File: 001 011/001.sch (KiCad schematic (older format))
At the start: 8 parts, among them J1 USB_C_Receptacle_USB2.0, J2 Conn_01x14, J3 Conn_01x12

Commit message: Updated 011 to have the hopefully correct schematic Still a split board bridge the tiny resistor pad for LED function on 001
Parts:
- removed R3, R4: Comp, Resistor_SMD:R_0603_1608Metric_Pad0.98x0.95mm_HandSolder, symbol Device:R
- added R5: Bridge for 001, Resistor_SMD:R_0201_0603Metric, symbol Device:R_Small
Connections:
- net VCC: now also J3.5 (Pin_5), J3.6 (Pin_6), R5.2; no longer D1.1, D1.2, D1.6, D1.7, J3.8 (Pin_8)
- net d+: now also J1.A6 (D+), J1.B6 (D+)
- net d-: now also J1.A7 (D-), J1.B7 (D-)
- new net Annode: D1.1, D1.2, D1.6, D1.7, J3.8 (Pin_8), R5.1
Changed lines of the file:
@@
-$EndComp
-$Comp
-L Connector_Generic:Conn_01x14 J2
-U 1 1 611858EF
-P 3700 1600
-F 0 "J2" H 3780 1592 50  0000 L CNN
-F 1 "Conn_01x14" H 3780 1501 50  0000 L CNN
-F 2 "Molex 503480-1400:503480-1400" H 3700 1600 50  0001 C CNN
-F 3 "~" H 3700 1600 50  0001 C CNN
-	1    3700 1600
-	1    0    0    -1
 $EndComp
 $Comp
@@
 	0    1    1    0
 $EndComp
-$Comp
-L Device:R R3
-U 1 1 61187F93
-P 2150 1500
-F 0 "R3" V 2050 1500 50  0000 C CNN
-F 1 "Comp" V 2150 1500 50  0000 C CNN
-F 2 "Resistor_SMD:R_0603_1608Metric_Pad0.98x0.95mm_HandSolder" V 2080 1500 50  0001 C CNN
-F 3 "~" H 2150 1500 50  0001 C CNN
-	1    2150 1500
-	0    1    1    0
-$EndComp
-$Comp
-L Device:R R4
-U 1 1 611891C9
-P 2150 1700
-F 0 "R4" V 2250 1700 50  0000 C CNN
-F 1 "Comp" V 2150 1700 50  0000 C CNN
-F 2 "Resistor_SMD:R_0603_1608Metric_Pad0.98x0.95mm_HandSolder" V 2080 1700 50  0001 C CNN
-F 3 "~" H 2150 1700 50  0001 C CNN
-	1    2150 1700
-	0    1    1    0
-$EndComp
-Text Label 2400 1500 0    50   ~ 0
+Text Label 1800 1500 0    50   ~ 0
 d-
-Text Label 2400 1700 0    50   ~ 0
+Text Label 1800 1700 0    50   ~ 0
 d+
-Wire Wire Line
-	1700 1450 1700 1500
-Wire Wire Line
-	2000 1500 1700 1500
-Connection ~ 1700 1500
-Wire Wire Line
-	1700 1500 1700 1550
-Wire Wire Line
-	1700 1650 1700 1700
-Wire Wire Line
-	2000 1700 1700 1700
-Connection ~ 1700 1700
-Wire Wire Line
-	1700 1700 1700 1750
-Wire Wire Line
-	2300 1700 2400 1700
-Wire Wire Line
-	2400 1500 2300 1500
 Wire Wire Line
 	1850 1150 1700 1150
@@
 Wire Wire Line
 	2300 2500 2350 2500
-Wire Wire Line
-	2450 2500 2450 2200
-Wire Wire Line
-	2550 2500 2550 2100
-Wire Wire Line
-	2650 2500 2650 2000
-Wire Wire Line
-	2450 2200 3500 2200
-Wire Wire Line
-	2550 2100 3500 2100
-Wire Wire Line
-	2650 2000 3500 2000
 $Comp
 L power:VCC #PWR08
@@
 L power:VCC #PWR07
 U 1 1 621AD55C
-P 2300 2300
-F 0 "#PWR07" H 2300 2150 50  0001 C CNN
-F 1 "VCC" H 2315 2473 50  0000 C CNN
-F 2 "" H 2300 2300 50  0001 C CNN
-F 3 "" H 2300 2300 50  0001 C CNN
-	1    2300 2300
+P 2300 2000
+F 0 "#PWR07" H 2300 1850 50  0001 C CNN
+F 1 "VCC" H 2400 2050 50  0000 C CNN
+F 2 "" H 2300 2000 50  0001 C CNN
+F 3 "" H 2300 2000 50  0001 C CNN
+	1    2300 2000
 	1    0    0    -1
 $EndComp
@@
 	4650 1450 4500 1450
 Wire Wire Line
-	4500 1450 4500 1550
+	4500 1450 4500 1500
 Wire Wire Line
 	4500 1550 4650 1550
@@
 L power:GND #PWR011
 U 1 1 6222D072
-P 4650 1650
-F 0 "#PWR011" H 4650 1400 50  0001 C CNN
-F 1 "GND" V 4655 1522 50  0000 R CNN
-F 2 "" H 4650 1650 50  0001 C CNN
-F 3 "" H 4650 1650 50  0001 C CNN
-	1    4650 1650
+P 4400 1650
+F 0 "#PWR011" H 4400 1400 50  0001 C CNN
+F 1 "GND" V 4350 1500 50  0000 R CNN
+F 2 "" H 4400 1650 50  0001 C CNN
+F 3 "" H 4400 1650 50  0001 C CNN
+	1    4400 1650
 	0    1    1    0
 $EndComp
@@
 L power:VCC #PWR012
 U 1 1 6222D542
-P 4650 1750
-F 0 "#PWR012" H 4650 1600 50  0001 C CNN
-F 1 "VCC" V 4665 1877 50  0000 L CNN
-F 2 "" H 4650 1750 50  0001 C CNN
-F 3 "" H 4650 1750 50  0001 C CNN
-	1    4650 1750
+P 4500 1500
+F 0 "#PWR012" H 4500 1350 50  0001 C CNN
+F 1 "VCC" V 4515 1627 50  0000 L CNN
+F 2 "" H 4500 1500 50  0001 C CNN
+F 3 "" H 4500 1500 50  0001 C CNN
+	1    4500 1500
 	0    -1   -1   0
 $EndComp
-Text Label 4650 1850 2    50   ~ 0
-G
 Text Label 4650 1950 2    50   ~ 0
 R
@@
 	0    1    1    0
 $EndComp
-Text Label 2650 2000 0    50   ~ 0
+Text Label 2650 2500 1    50   ~ 0
 G
-Text Label 2550 2100 0    50   ~ 0
+Text Label 2550 2500 1    50   ~ 0
 R
-Text Label 2450 2200 0    50   ~ 0
+Text Label 2450 2500 1    50   ~ 0
 B
+$Comp
+L Device:R_Small R5
+U 1 1 625509C5
+P 2300 2150
+F 0 "R5" V 2300 2200 50  0000 R CNN
+F 1 "Bridge for 001" V 2400 2400 50  0000 R CNN
+F 2 "Resistor_SMD:R_0201_0603Metric" H 2300 2150 50  0001 C CNN
+F 3 "~" H 2300 2150 50  0001 C CNN
+	1    2300 2150
+	-1   0    0    1
+$EndComp
+Wire Wire Line
+	2300 2250 2300 2300
+Wire Wire Line
+	2300 2000 2300 2050
+Text Label 2450 2300 0    50   ~ 0
+Annode
+Connection ~ 4500 1500
+Wire Wire Line
+	4500 1500 4500 1550
+Text Label 4650 1750 2    50   ~ 0
+Annode
+Text Label 4650 1850 2    50   ~ 0
+G
+Wire Wire Line
+	4400 1650 4650 1650
+Wire Wire Line
+	1700 1450 1700 1500
+Wire Wire Line
+	1700 1650 1700 1700
+Wire Wire Line
+	1800 1500 1700 1500
+Connection ~ 1700 1500
+Wire Wire Line
+	1700 1500 1700 1550
+Wire Wire Line
+	1800 1700 1700 1700
+Connection ~ 1700 1700
+Wire Wire Line
+	1700 1700 1700 1750
+Text Label 3500 2200 2    50   ~ 0
+B
+Text Label 3500 2100 2    50   ~ 0
+R
+Text Label 3500 2000 2    50   ~ 0
+G
+$Comp
+L Connector_Generic:Conn_01x14 J2
+U 1 1 611858EF
+P 3700 1600
+F 0 "J2" H 3780 1592 50  0000 L CNN
+F 1 "Conn_01x14" H 3780 1501 50  0000 L CNN
+F 2 "Molex 503480-1400:503480-1400" H 3700 1600 50  0001 C CNN
+F 3 "~" H 3700 1600 50  0001 C CNN
+	1    3700 1600
+	1    0    0    -1
+$EndComp
 $EndSCHEMATC

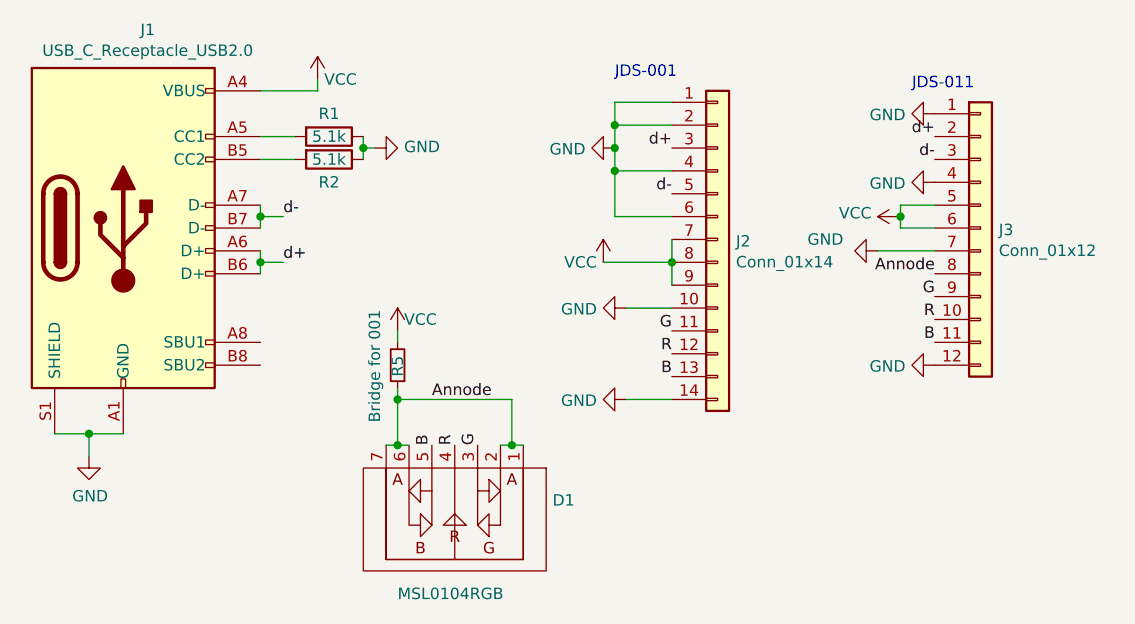
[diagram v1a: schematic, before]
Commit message: 001, 011, 030 standardized to a cheaper LED
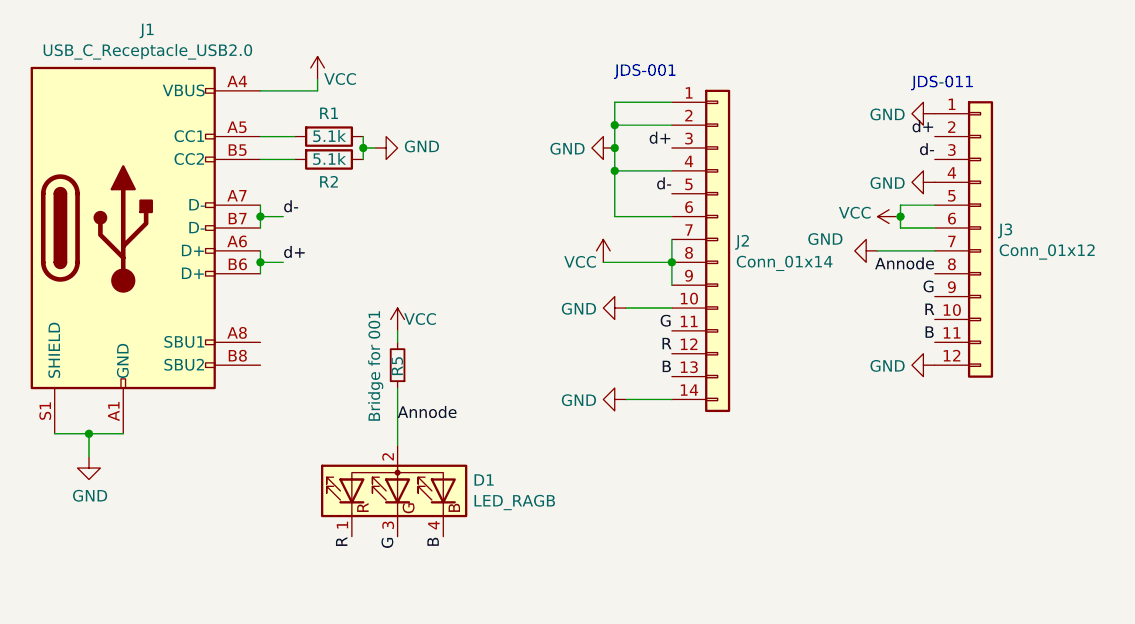
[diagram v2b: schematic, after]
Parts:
- removed D1: MSL0104RGB, MSL0104RGB:MSL0104RGB, symbol MSL0104RGB:MSL0104RGB
- added D1: LED_RAGB, New_LED:FM-3510RGBA-SG, symbol Device:LED_RAGB
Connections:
- net Annode: now also D1.2 (A)
- net B: now also D1.4 (BK)
- net G: now also D1.3 (GK)
- net R: now also D1.1 (RK)
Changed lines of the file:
@@
 	3500 2300 3300 2300
-$Comp
-L MSL0104RGB:MSL0104RGB D1
-U 1 1 6119707E
-P 2550 2650
-F 0 "D1" H 2122 2741 50  0000 R CNN
-F 1 "MSL0104RGB" H 2800 3150 50  0000 R CNN
-F 2 "MSL0104RGB:MSL0104RGB" H 2550 2650 50  0001 C CNN
-F 3 "" H 2550 2650 50  0001 C CNN
-	1    2550 2650
-	-1   0    0    1
-$EndComp
-Wire Wire Line
-	2850 2500 2800 2500
-Wire Wire Line
-	2250 2500 2300 2500
-Wire Wire Line
-	2800 2500 2800 2300
-Wire Wire Line
-	2800 2300 2300 2300
-Wire Wire Line
-	2300 2300 2300 2500
-Connection ~ 2800 2500
-Wire Wire Line
-	2800 2500 2750 2500
-Connection ~ 2300 2500
-Wire Wire Line
-	2300 2500 2350 2500
 $Comp
 L power:VCC #PWR08
@@
 	1    0    0    -1
 $EndComp
-Connection ~ 2300 2300
 $Comp
 L power:VCC #PWR06
@@
 	0    1    1    0
 $EndComp
-Text Label 2650 2500 1    50   ~ 0
+Text Label 2300 2900 3    50   ~ 0
 G
-Text Label 2550 2500 1    50   ~ 0
+Text Label 2100 2900 3    50   ~ 0
 R
-Text Label 2450 2500 1    50   ~ 0
+Text Label 2500 2900 3    50   ~ 0
 B
 $Comp
@@
 $EndComp
 Wire Wire Line
-	2300 2250 2300 2300
-Wire Wire Line
 	2300 2000 2300 2050
-Text Label 2450 2300 0    50   ~ 0
+Text Label 2300 2400 0    50   ~ 0
 Annode
 Connection ~ 4500 1500
@@
 	1    0    0    -1
 $EndComp
+$Comp
+L Device:LED_RAGB D1
+U 1 1 625CBE9C
+P 2300 2700
+F 0 "D1" V 2346 2370 50  0000 R CNN
+F 1 "LED_RAGB" V 2255 2370 50  0000 R CNN
+F 2 "New_LED:FM-3510RGBA-SG" H 2300 2650 50  0001 C CNN
+F 3 "~" H 2300 2650 50  0001 C CNN
+	1    2300 2700
+	0    -1   -1   0
+$EndComp
+Wire Wire Line
+	2300 2250 2300 2500
 $EndSCHEMATC
